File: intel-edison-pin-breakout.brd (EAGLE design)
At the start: 97.5 x 99 mm, 5 parts, among them U1 EDISON_CONNECTOR_FULLMOUNTING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

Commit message: board width
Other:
- board size 97.5 x 99 mm -> 94.9 x 99 mm
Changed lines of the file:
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@@
 <board>
 <plain>
-<wire x1="0" y1="-5.08" x2="97.46" y2="-5.08" width="0" layer="20"/>
-<wire x1="97.46" y1="-5.08" x2="97.46" y2="93.97" width="0" layer="20"/>
-<wire x1="97.46" y1="93.97" x2="0" y2="93.97" width="0" layer="20"/>
+<wire x1="0" y1="-5.08" x2="94.92" y2="-5.08" width="0" layer="20"/>
+<wire x1="94.92" y1="-5.08" x2="94.92" y2="93.97" width="0" layer="20"/>
+<wire x1="94.92" y1="93.97" x2="0" y2="93.97" width="0" layer="20"/>
 <wire x1="0" y1="93.97" x2="0" y2="-5.08" width="0" layer="20"/>
 </plain>

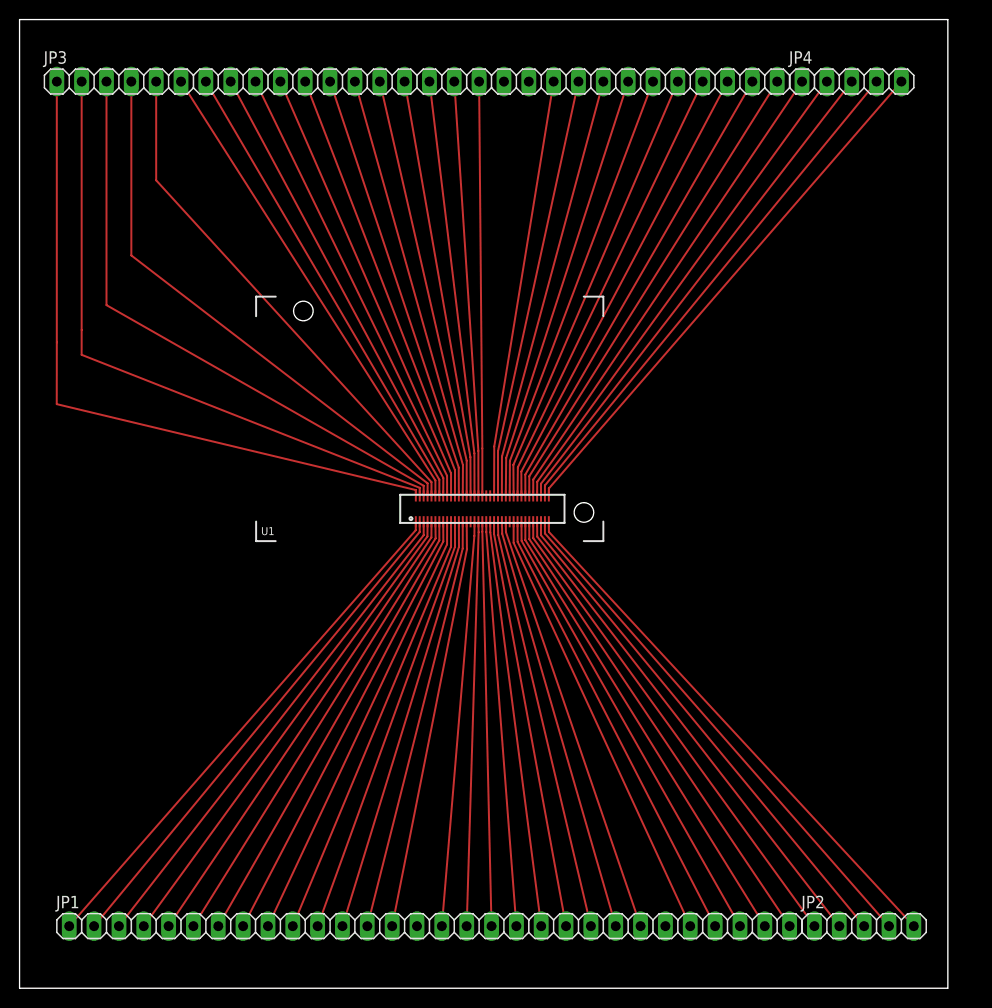
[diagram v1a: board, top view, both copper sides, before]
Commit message: reduce board size
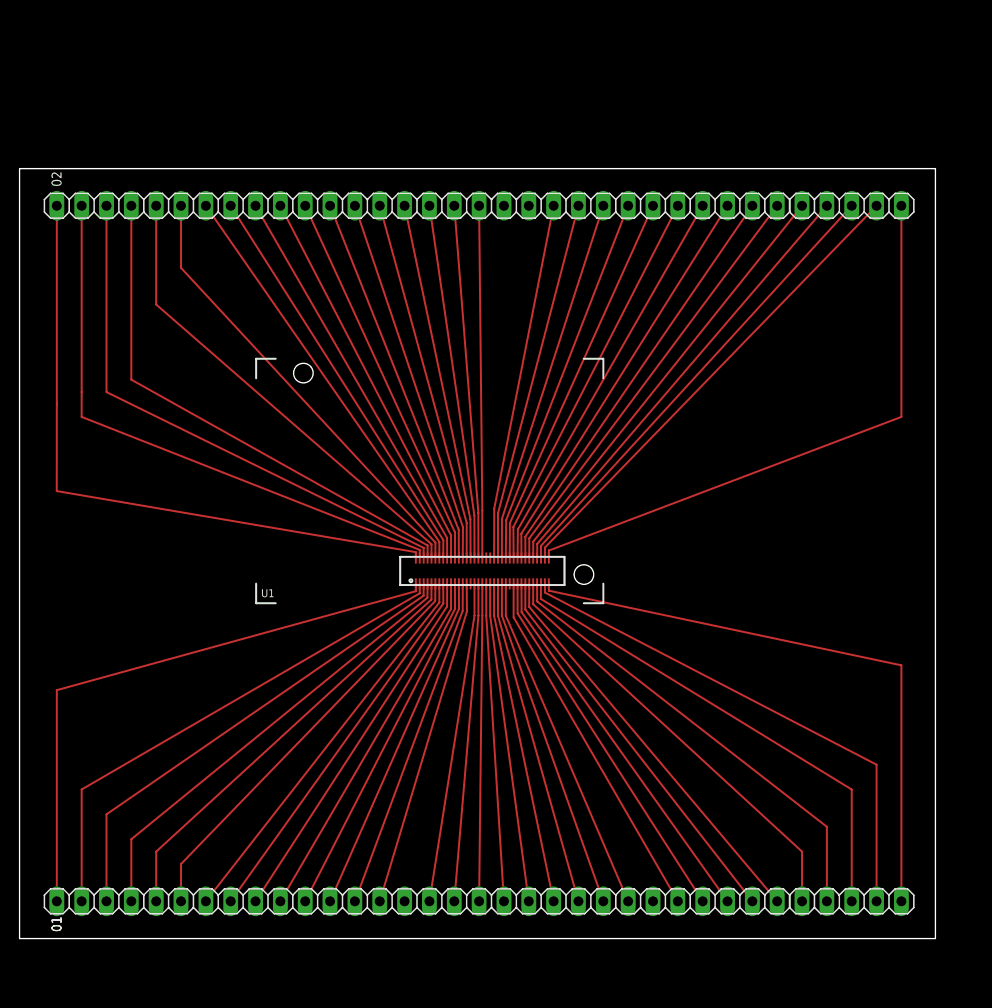
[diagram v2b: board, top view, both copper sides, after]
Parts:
- moved JP3 12.7 mm to (40.6, 74.9)
- moved JP4 12.7 mm to (85.1, 74.9)
- moved U1 6.35 mm to (59.7, 34.3)
- moved JP1 2.84 mm to (40.6, 3.81)
- moved JP2 2.84 mm to (85.1, 3.81)
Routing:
- net N$18: track 41.7 -> 32.7 mm
- net N$17: track 41.5 -> 32.5 mm
- net N$19: track 42.0 -> 33.1 mm
- net N$16: track 41.4 -> 32.5 mm
- net N$20: track 42.5 -> 33.6 mm
- net N$14: track 41.4 -> 32.6 mm
- net N$21: track 43.0 -> 34.2 mm
- net N$15: track 41.5 -> 32.8 mm
- net N$22: track 43.6 -> 35.0 mm
- net N$23: track 45.3 -> 37.0 mm
- net N$28: track 42.1 -> 33.8 mm
- net N$24: track 46.2 -> 38.0 mm
- net N$13: track 42.6 -> 34.4 mm
- net N$25: track 47.2 -> 39.2 mm
- net N$12: track 43.1 -> 35.2 mm
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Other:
- board size 94.9 x 99 mm -> 93.7 x 78.7 mm
- board text added: "01"
- board text added: "02"

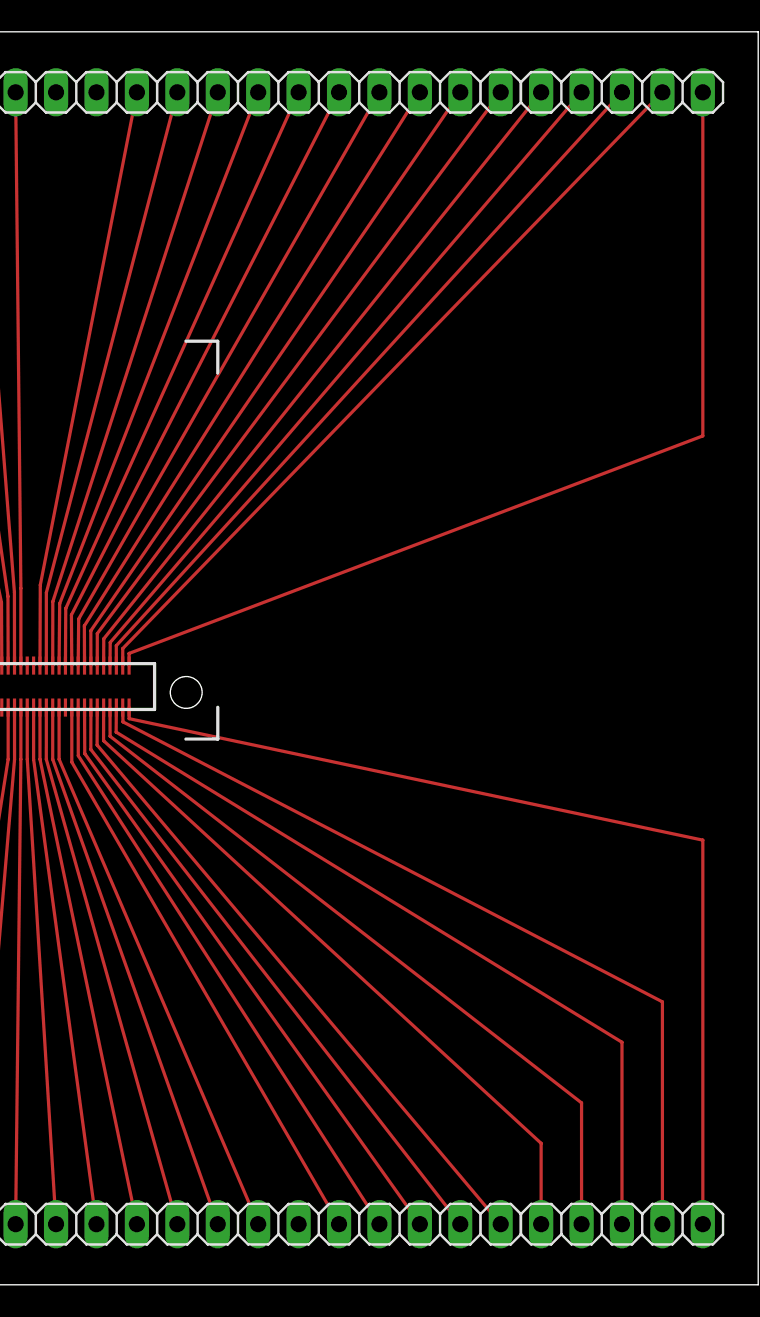
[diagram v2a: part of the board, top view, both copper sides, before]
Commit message: last 6 wires of each corner have edges
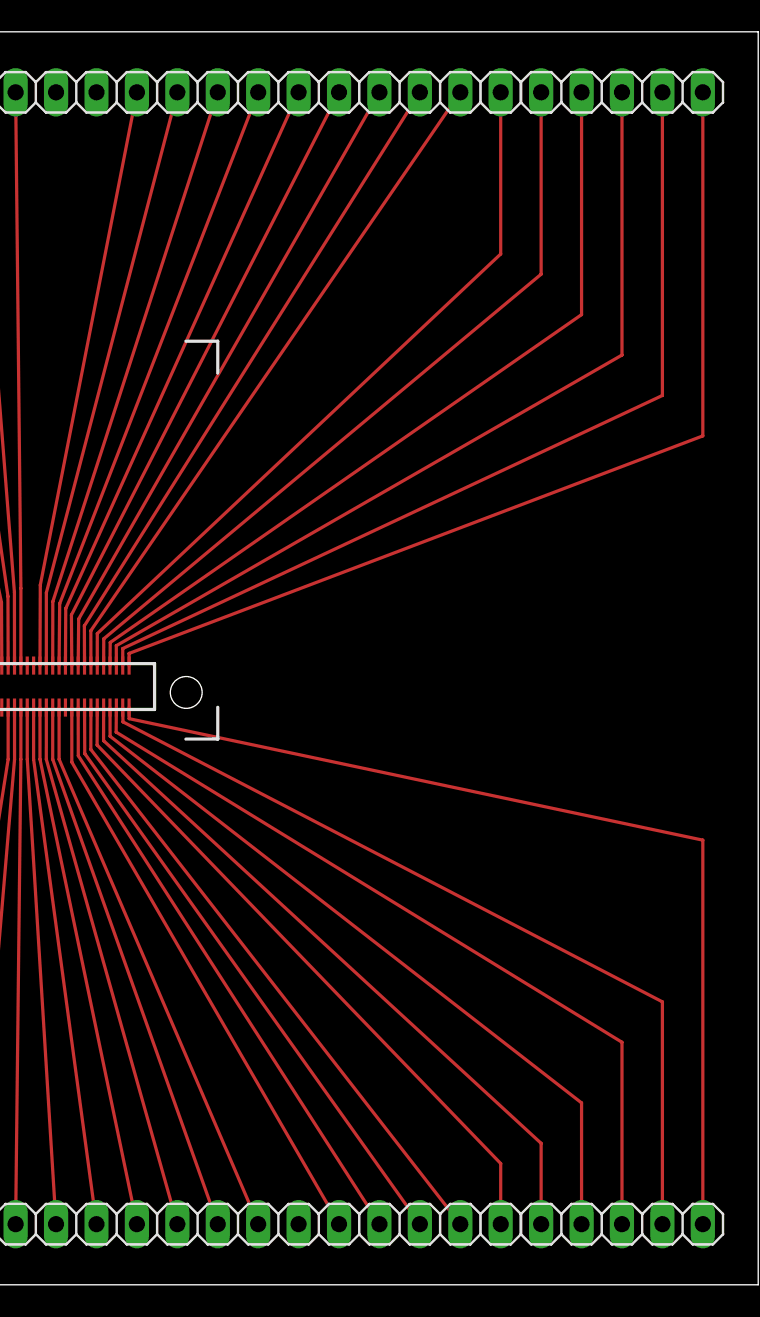
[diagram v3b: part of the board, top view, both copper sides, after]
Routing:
- net N$54: track 49.8 -> 57.6 mm
- net N$56: track 48.4 -> 54.4 mm
- net N$57: track 47.0 -> 51.5 mm
- net N$58: track 45.7 -> 48.9 mm
- net N$59: track 44.4 -> 47.0 mm
- net N$27: track 41.7 -> 42.7 mm
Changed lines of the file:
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@@
 <contactref element="JP4" pad="4"/>
 <wire x1="53.72" y1="38.91" x2="53.721" y2="39.9796" width="0.2032" layer="1"/>
-<wire x1="53.721" y1="39.9796" x2="87.63" y2="74.93" width="0.2032" layer="1"/>
+<wire x1="87.63" y1="74.93" x2="87.63" y2="55.88" width="0.2032" layer="1"/>
+<wire x1="87.63" y1="55.88" x2="53.721" y2="39.9796" width="0.2032" layer="1"/>
 </signal>
 <signal name="N$56">
@@
 <contactref element="JP4" pad="3"/>
 <wire x1="53.32" y1="38.91" x2="53.3146" y2="40.1574" width="0.2032" layer="1"/>
-<wire x1="53.3146" y1="40.1574" x2="85.09" y2="74.93" width="0.2032" layer="1"/>
+<wire x1="85.09" y1="74.93" x2="85.09" y2="58.42" width="0.2032" layer="1"/>
+<wire x1="85.09" y1="58.42" x2="53.3146" y2="40.1574" width="0.2032" layer="1"/>
 </signal>
 <signal name="N$57">
@@
 <contactref element="JP4" pad="2"/>
 <wire x1="52.92" y1="38.91" x2="52.9336" y2="40.3606" width="0.2032" layer="1"/>
-<wire x1="52.9336" y1="40.3606" x2="82.55" y2="74.93" width="0.2032" layer="1"/>
+<wire x1="82.55" y1="74.93" x2="82.55" y2="60.96" width="0.2032" layer="1"/>
+<wire x1="82.55" y1="60.96" x2="52.9336" y2="40.3606" width="0.2032" layer="1"/>
 </signal>
 <signal name="N$58">
@@
 <contactref element="JP4" pad="1"/>
 <wire x1="52.52" y1="38.91" x2="52.5272" y2="40.5892" width="0.2032" layer="1"/>
-<wire x1="52.5272" y1="40.5892" x2="80.01" y2="74.93" width="0.2032" layer="1"/>
+<wire x1="52.5272" y1="40.5892" x2="80.01" y2="63.5" width="0.2032" layer="1"/>
+<wire x1="80.01" y1="63.5" x2="80.01" y2="74.93" width="0.2032" layer="1"/>
 </signal>
 <signal name="N$59">
@@
 <contactref element="JP3" pad="30"/>
 <wire x1="52.12" y1="38.91" x2="52.1208" y2="40.9194" width="0.2032" layer="1"/>
-<wire x1="52.1208" y1="40.9194" x2="77.47" y2="74.93" width="0.2032" layer="1"/>
+<wire x1="77.47" y1="74.93" x2="77.47" y2="64.77" width="0.2032" layer="1"/>
+<wire x1="77.47" y1="64.77" x2="52.1208" y2="40.9194" width="0.2032" layer="1"/>
 </signal>
 <signal name="N$60">
@@
 <contactref element="JP1" pad="30"/>
 <wire x1="52.12" y1="36.27" x2="52.10936875" y2="33.917890625" width="0.2032" layer="1"/>
-<wire x1="52.10936875" y1="33.917890625" x2="77.47" y2="3.81" width="0.2032" layer="1"/>
+<wire x1="77.47" y1="3.81" x2="77.47" y2="7.62" width="0.2032" layer="1"/>
+<wire x1="77.47" y1="7.62" x2="52.10936875" y2="33.917890625" width="0.2032" layer="1"/>
 </signal>
 <signal name="N$20">

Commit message: don't bend the last wire so much
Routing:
- net N$33: track 61.7 -> 56.3 mm
- net N$1: track 60.4 -> 55.5 mm
- net N$34: track 67.0 -> 63.1 mm
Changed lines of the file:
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@@
 <contactref element="JP1" pad="1"/>
 <wire x1="40.52" y1="36.27" x2="40.518078125" y2="35.51681875" width="0.2032" layer="1"/>
-<wire x1="3.81" y1="3.81" x2="3.81" y2="25.4" width="0.2032" layer="1"/>
-<wire x1="3.81" y1="25.4" x2="40.518078125" y2="35.51681875" width="0.2032" layer="1"/>
+<wire x1="3.81" y1="3.81" x2="3.81" y2="17.78" width="0.2032" layer="1"/>
+<wire x1="3.81" y1="17.78" x2="40.518078125" y2="35.51681875" width="0.2032" layer="1"/>
 </signal>
 <signal name="N$2">
@@
 <contactref element="JP2" pad="5"/>
 <wire x1="54.12" y1="36.27" x2="54.12231875" y2="35.5727" width="0.2032" layer="1"/>
-<wire x1="54.12231875" y1="35.5727" x2="90.17" y2="27.94" width="0.2032" layer="1"/>
-<wire x1="90.17" y1="3.81" x2="90.17" y2="27.94" width="0.2032" layer="1"/>
+<wire x1="54.12231875" y1="35.5727" x2="90.17" y2="20.32" width="0.2032" layer="1"/>
+<wire x1="90.17" y1="3.81" x2="90.17" y2="20.32" width="0.2032" layer="1"/>
 </signal>
 <signal name="N$34">
@@
 <wire x1="40.52" y1="38.91" x2="40.521890625" y2="39.512240625" width="0.2032" layer="1"/>
 <wire x1="3.81" y1="54.61" x2="3.81" y2="74.93" width="0.2032" layer="1"/>
-<wire x1="3.81" y1="54.61" x2="3.803759375" y2="45.75555625" width="0.2032" layer="1"/>
-<wire x1="40.521890625" y1="39.512240625" x2="3.803759375" y2="45.75555625" width="0.2032" layer="1"/>
+<wire x1="3.81" y1="54.61" x2="3.803759375" y2="50.83555625" width="0.2032" layer="1"/>
+<wire x1="40.521890625" y1="39.512240625" x2="3.803759375" y2="50.83555625" width="0.2032" layer="1"/>
 </signal>
 <signal name="N$35">

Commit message: wires
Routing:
- net N$53: track 60.9 -> 52.0 mm
- net N$34: track 63.1 -> 54.3 mm
- net N$54: track 57.6 -> 50.5 mm
- net N$35: track 59.6 -> 52.6 mm
- net N$56: track 54.4 -> 49.0 mm
- net N$36: track 56.2 -> 51.1 mm
- net N$37: track 53.8 -> 49.6 mm
- net N$57: track 51.5 -> 47.6 mm
- net N$58: track 48.9 -> 46.3 mm
- net N$59: track 47.0 -> 45.0 mm
- net N$38: track 48.8 -> 48.0 mm
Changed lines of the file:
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@@
 <contactref element="JP3" pad="1"/>
 <wire x1="40.52" y1="38.91" x2="40.521890625" y2="39.512240625" width="0.2032" layer="1"/>
-<wire x1="3.81" y1="54.61" x2="3.81" y2="74.93" width="0.2032" layer="1"/>
-<wire x1="3.81" y1="54.61" x2="3.803759375" y2="50.83555625" width="0.2032" layer="1"/>
-<wire x1="40.521890625" y1="39.512240625" x2="3.803759375" y2="50.83555625" width="0.2032" layer="1"/>
+<wire x1="40.521890625" y1="39.512240625" x2="3.803759375" y2="67.34555625" width="0.2032" layer="1"/>
+<wire x1="3.81" y1="74.93" x2="3.803759375" y2="67.34555625" width="0.2032" layer="1"/>
 </signal>
 <signal name="N$35">
 <contactref element="U1" pad="4"/>
 <contactref element="JP3" pad="2"/>
-<wire x1="6.35" y1="55.88" x2="6.35" y2="74.93" width="0.2032" layer="1"/>
-<wire x1="40.92" y1="38.91" x2="40.92448125" y2="39.7383" width="0.2032" layer="1"/>
-<wire x1="6.35" y1="55.88" x2="6.348228125" y2="53.34" width="0.2032" layer="1"/>
-<wire x1="40.92448125" y1="39.7383" x2="6.348228125" y2="53.34" width="0.2032" layer="1"/>
+<wire x1="6.35" y1="74.93" x2="6.35" y2="67.31" width="0.2032" layer="1"/>
+<wire x1="40.92" y1="38.91" x2="40.91813125" y2="39.69511875" width="0.2032" layer="1"/>
+<wire x1="40.91813125" y1="39.69511875" x2="6.35" y2="67.31" width="0.2032" layer="1"/>
 </signal>
 <signal name="N$36">
 <contactref element="U1" pad="6"/>
 <contactref element="JP3" pad="3"/>
-<wire x1="8.89" y1="74.93" x2="8.89" y2="55.88" width="0.2032" layer="1"/>
+<wire x1="8.89" y1="74.93" x2="8.89" y2="67.31" width="0.2032" layer="1"/>
 <wire x1="41.32" y1="38.91" x2="41.31945" y2="39.950390625" width="0.2032" layer="1"/>
-<wire x1="41.31945" y1="39.950390625" x2="8.89" y2="55.88" width="0.2032" layer="1"/>
+<wire x1="41.31945" y1="39.950390625" x2="8.89" y2="67.31" width="0.2032" layer="1"/>
 </signal>
 <signal name="N$37">
 <contactref element="U1" pad="8"/>
 <contactref element="JP3" pad="4"/>
-<wire x1="11.43" y1="74.93" x2="11.43" y2="57.15" width="0.2032" layer="1"/>
+<wire x1="11.43" y1="74.93" x2="11.43" y2="67.31" width="0.2032" layer="1"/>
 <wire x1="41.72" y1="38.91" x2="41.72585" y2="40.19676875" width="0.2032" layer="1"/>
-<wire x1="41.72585" y1="40.19676875" x2="11.43" y2="57.15" width="0.2032" layer="1"/>
+<wire x1="41.72585" y1="40.19676875" x2="11.43" y2="67.31" width="0.2032" layer="1"/>
 </signal>
 <signal name="N$38">
@@
 <wire x1="42.12" y1="38.91" x2="42.11828125" y2="38.91" width="0.2032" layer="1"/>
 <wire x1="42.12" y1="38.91" x2="42.12081875" y2="40.325040625" width="0.2032" layer="1"/>
-<wire x1="13.97" y1="64.83223125" x2="13.97" y2="74.93" width="0.2032" layer="1"/>
-<wire x1="42.12081875" y1="40.325040625" x2="13.97" y2="64.83223125" width="0.2032" layer="1"/>
+<wire x1="13.97" y1="67.37223125" x2="13.97" y2="74.93" width="0.2032" layer="1"/>
+<wire x1="42.12081875" y1="40.325040625" x2="13.97" y2="67.37223125" width="0.2032" layer="1"/>
 </signal>
 <signal name="N$39">
@@
 <contactref element="JP3" pad="6"/>
 <wire x1="42.52" y1="38.91" x2="42.522140625" y2="40.48886875" width="0.2032" layer="1"/>
-<wire x1="16.51" y1="74.93" x2="16.51" y2="68.58" width="0.2032" layer="1"/>
-<wire x1="16.51" y1="68.58" x2="42.522140625" y2="40.48886875" width="0.2032" layer="1"/>
+<wire x1="16.51" y1="74.93" x2="16.51" y2="67.31" width="0.2032" layer="1"/>
+<wire x1="16.51" y1="67.31" x2="42.522140625" y2="40.48886875" width="0.2032" layer="1"/>
 </signal>
 <signal name="N$40">
@@
 <wire x1="54.12" y1="38.91" x2="54.12" y2="39.6674" width="0.2032" layer="1"/>
 <wire x1="54.12" y1="39.6674" x2="54.1274" y2="39.6748" width="0.2032" layer="1"/>
-<wire x1="90.17" y1="74.93" x2="90.17" y2="53.34" width="0.2032" layer="1"/>
-<wire x1="90.17" y1="53.34" x2="54.1274" y2="39.6748" width="0.2032" layer="1"/>
+<wire x1="90.17" y1="74.93" x2="90.17" y2="72.39" width="0.2032" layer="1"/>
+<wire x1="90.17" y1="72.39" x2="54.1274" y2="39.6748" width="0.2032" layer="1"/>
 </signal>
 <signal name="N$54">
@@
 <contactref element="JP4" pad="4"/>
 <wire x1="53.72" y1="38.91" x2="53.721" y2="39.9796" width="0.2032" layer="1"/>
-<wire x1="87.63" y1="74.93" x2="87.63" y2="55.88" width="0.2032" layer="1"/>
-<wire x1="87.63" y1="55.88" x2="53.721" y2="39.9796" width="0.2032" layer="1"/>
+<wire x1="87.63" y1="74.93" x2="87.63" y2="72.39" width="0.2032" layer="1"/>
+<wire x1="87.63" y1="72.39" x2="53.721" y2="39.9796" width="0.2032" layer="1"/>
 </signal>
 <signal name="N$56">
@@
 <contactref element="JP4" pad="3"/>
 <wire x1="53.32" y1="38.91" x2="53.3146" y2="40.1574" width="0.2032" layer="1"/>
-<wire x1="85.09" y1="74.93" x2="85.09" y2="58.42" width="0.2032" layer="1"/>
-<wire x1="85.09" y1="58.42" x2="53.3146" y2="40.1574" width="0.2032" layer="1"/>
+<wire x1="85.09" y1="74.93" x2="85.09" y2="72.39" width="0.2032" layer="1"/>
+<wire x1="85.09" y1="72.39" x2="53.3146" y2="40.1574" width="0.2032" layer="1"/>
 </signal>
 <signal name="N$57">
@@
 <contactref element="JP4" pad="2"/>
 <wire x1="52.92" y1="38.91" x2="52.9336" y2="40.3606" width="0.2032" layer="1"/>
-<wire x1="82.55" y1="74.93" x2="82.55" y2="60.96" width="0.2032" layer="1"/>
-<wire x1="82.55" y1="60.96" x2="52.9336" y2="40.3606" width="0.2032" layer="1"/>
+<wire x1="82.55" y1="74.93" x2="82.55" y2="72.39" width="0.2032" layer="1"/>
+<wire x1="82.55" y1="72.39" x2="52.9336" y2="40.3606" width="0.2032" layer="1"/>
 </signal>
 <signal name="N$58">
@@
 <contactref element="JP4" pad="1"/>
 <wire x1="52.52" y1="38.91" x2="52.5272" y2="40.5892" width="0.2032" layer="1"/>
-<wire x1="52.5272" y1="40.5892" x2="80.01" y2="63.5" width="0.2032" layer="1"/>
-<wire x1="80.01" y1="63.5" x2="80.01" y2="74.93" width="0.2032" layer="1"/>
+<wire x1="52.5272" y1="40.5892" x2="80.01" y2="72.39" width="0.2032" layer="1"/>
+<wire x1="80.01" y1="72.39" x2="80.01" y2="74.93" width="0.2032" layer="1"/>
 </signal>
 <signal name="N$59">
@@
 <contactref element="JP3" pad="30"/>
 <wire x1="52.12" y1="38.91" x2="52.1208" y2="40.9194" width="0.2032" layer="1"/>
-<wire x1="77.47" y1="74.93" x2="77.47" y2="64.77" width="0.2032" layer="1"/>
-<wire x1="77.47" y1="64.77" x2="52.1208" y2="40.9194" width="0.2032" layer="1"/>
+<wire x1="77.47" y1="74.93" x2="77.47" y2="72.39" width="0.2032" layer="1"/>
+<wire x1="77.47" y1="72.39" x2="52.1208" y2="40.9194" width="0.2032" layer="1"/>
 </signal>
 <signal name="N$60">
